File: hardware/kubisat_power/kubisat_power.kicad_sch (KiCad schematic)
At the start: 79 parts, among them J1 USB_C_Receptacle_PowerOnly_6P, Q1 Si2305, SW1 SW_Wuerth_450301014042, U1 TPS79601DCQ, U2 INA3221, U3 LN2220, U4 CN3791, U5 TP4056, U6 DW01A, U7 FS8205

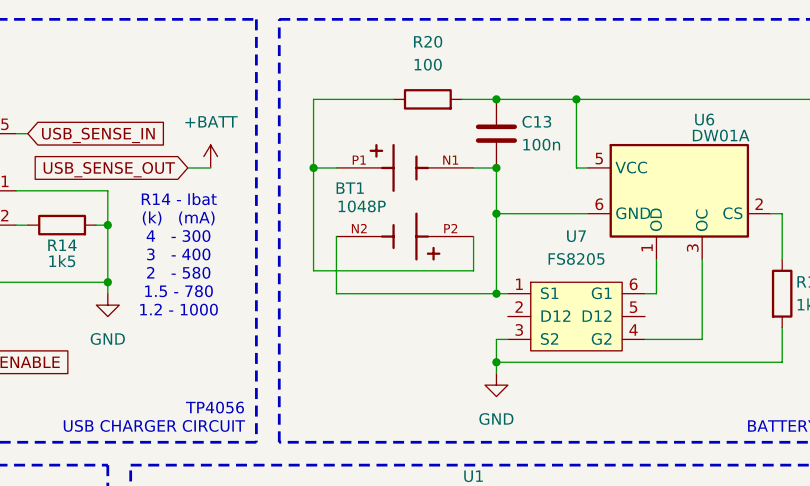
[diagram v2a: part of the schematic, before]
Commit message: changed battery holder
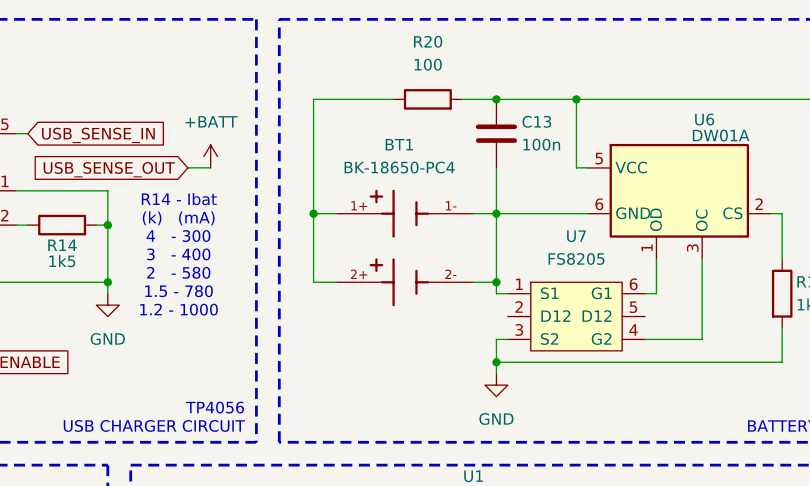
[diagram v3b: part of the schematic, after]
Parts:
- removed BT1: 1048P, 1048P:BAT_1048P, symbol 1048P:1048P
- added BT1: BK-18650-PC4, BK-18650-PC4:BAT_BK-18650-PC4, symbol kubisat:BK-18650-PC4
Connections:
- net at C13.2, U6.6 (GND), U7.1 (S1): now also BT1.1-, BT1.2-
- net at R20.1: now also BT1.1+, BT1.2+
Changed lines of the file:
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@@
 	)
 	(junction
+		(at 167.64 44.45)
+		(diameter 0)
+		(color 0 0 0 0)
+	)
+	(junction
 		(at 252.73 77.47)
 		(diameter 0)
@@
 	)
 	(junction
-		(at 147.32 31.75)
-		(diameter 0)
-		(color 0 0 0 0)
-	)
-	(junction
 		(at 165.1 88.9)
 		(diameter 0)
@@
 	)
 	(junction
-		(at 167.64 31.75)
-		(diameter 0)
-		(color 0 0 0 0)
-	)
-	(junction
 		(at 243.84 107.95)
 		(diameter 0)
@@
 	)
 	(junction
+		(at 147.32 36.83)
+		(diameter 0)
+		(color 0 0 0 0)
+	)
+	(junction
 		(at 259.08 27.94)
 		(diameter 0)
@@
 	)
 	(junction
-		(at 167.64 45.72)
-		(diameter 0)
-		(color 0 0 0 0)
-	)
-	(junction
 		(at 238.76 115.57)
 		(diameter 0)
@@
 	(wire
 		(pts
+			(xy 167.64 44.45) (xy 167.64 45.72)
+		)
+		(stroke
+			(width 0)
+			(type default)
+		)
+	)
+	(wire
+		(pts
 			(xy 214.63 137.16) (xy 212.09 137.16)
 		)
@@
 	(wire
 		(pts
-			(xy 167.64 45.72) (xy 149.86 45.72)
-		)
-		(stroke
-			(width 0)
-			(type default)
-		)
-	)
-	(wire
-		(pts
 			(xy 222.25 39.37) (xy 222.25 41.91)
 		)
@@
 	(wire
 		(pts
-			(xy 149.86 45.72) (xy 149.86 39.37)
-		)
-		(stroke
-			(width 0)
-			(type default)
-		)
-	)
-	(wire
-		(pts
 			(xy 53.34 111.76) (xy 53.34 115.57)
 		)
@@
 	(wire
 		(pts
+			(xy 147.32 44.45) (xy 149.86 44.45)
+		)
+		(stroke
+			(width 0)
+			(type default)
+		)
+	)
+	(wire
+		(pts
 			(xy 168.91 154.94) (xy 168.91 153.67)
 		)
@@
 	(wire
 		(pts
+			(xy 165.1 44.45) (xy 167.64 44.45)
+		)
+		(stroke
+			(width 0)
+			(type default)
+		)
+	)
+	(wire
+		(pts
 			(xy 67.31 54.61) (xy 67.31 52.07)
 		)
@@
 	(wire
 		(pts
-			(xy 147.32 31.75) (xy 147.32 24.13)
+			(xy 147.32 24.13) (xy 147.32 36.83)
 		)
 		(stroke
@@
 	(wire
 		(pts
-			(xy 147.32 43.18) (xy 165.1 43.18)
-		)
-		(stroke
-			(width 0)
-			(type default)
-		)
-	)
-	(wire
-		(pts
 			(xy 168.91 144.78) (xy 168.91 146.05)
 		)
@@
 	(wire
 		(pts
-			(xy 165.1 31.75) (xy 167.64 31.75)
-		)
-		(stroke
-			(width 0)
-			(type default)
-		)
-	)
-	(wire
-		(pts
 			(xy 233.68 154.94) (xy 238.76 154.94)
 		)
@@
 	(wire
 		(pts
+			(xy 147.32 36.83) (xy 147.32 44.45)
+		)
+		(stroke
+			(width 0)
+			(type default)
+		)
+	)
+	(wire
+		(pts
 			(xy 87.63 72.39) (xy 88.9 72.39)
 		)
@@
 	(wire
 		(pts
-			(xy 165.1 39.37) (xy 165.1 43.18)
-		)
-		(stroke
-			(width 0)
-			(type default)
-		)
-	)
-	(wire
-		(pts
-			(xy 167.64 36.83) (xy 167.64 45.72)
-		)
-		(stroke
-			(width 0)
-			(type default)
-		)
-	)
-	(wire
-		(pts
 			(xy 176.53 146.05) (xy 168.91 146.05)
 		)
@@
 	(wire
 		(pts
-			(xy 147.32 31.75) (xy 147.32 43.18)
-		)
-		(stroke
-			(width 0)
-			(type default)
-		)
-	)
-	(wire
-		(pts
 			(xy 205.74 22.86) (xy 205.74 24.13)
 		)
@@
 	(wire
 		(pts
-			(xy 167.64 31.75) (xy 167.64 36.83)
-		)
-		(stroke
-			(width 0)
-			(type default)
-		)
-	)
-	(wire
-		(pts
 			(xy 119.38 73.66) (xy 119.38 76.2)
 		)
@@
 	(wire
 		(pts
-			(xy 149.86 31.75) (xy 147.32 31.75)
+			(xy 149.86 36.83) (xy 147.32 36.83)
 		)
 		(stroke
@@
 	(wire
 		(pts
+			(xy 165.1 36.83) (xy 167.64 36.83)
+		)
+		(stroke
+			(width 0)
+			(type default)
+		)
+	)
+	(wire
+		(pts
 			(xy 180.34 128.27) (xy 179.07 128.27)
 		)
@@
 	(wire
 		(pts
+			(xy 167.64 36.83) (xy 167.64 31.75)
+		)
+		(stroke
+			(width 0)
+			(type default)
+		)
+	)
+	(wire
+		(pts
 			(xy 238.76 154.94) (xy 238.76 151.13)
 		)
@@
 	(wire
 		(pts
+			(xy 167.64 36.83) (xy 167.64 44.45)
+		)
+		(stroke
+			(width 0)
+			(type default)
+		)
+	)
+	(wire
+		(pts
 			(xy 278.13 26.67) (xy 278.13 30.48)
 		)
@@
 	)
 	(symbol
-		(lib_id "1048P:1048P")
-		(at 157.48 34.29 0)
+		(lib_id "kubisat:BK-18650-PC4")
+		(at 157.48 39.37 0)
 		(unit 1)
 		(exclude_from_sim no)
@@
 		(on_board yes)
 		(dnp no)
+		(fields_autoplaced yes)
 		(property "Reference" "BT1"
-			(at 151.384 34.036 0)
+			(at 156.845 29.21 0)
 			(effects
 				(font
@@
 			)
 		)
-		(property "Value" "1048P"
-			(at 152.654 36.068 0)
+		(property "Value" "BK-18650-PC4"
+			(at 156.845 31.75 0)
 			(effects
 				(font
@@
 			)
 		)
-		(property "Footprint" "1048P:BAT_1048P"
-			(at 157.48 34.29 0)
+		(property "Footprint" "BK-18650-PC4:BAT_BK-18650-PC4"
+			(at 157.48 39.37 0)
 			(effects
 				(font
@@
 		)
 		(property "Datasheet" ""
-			(at 157.48 34.29 0)
+			(at 157.48 39.37 0)
 			(effects
 				(font
@@
 		)
 		(property "Description" ""
-			(at 157.48 34.29 0)
+			(at 157.48 39.37 0)
 			(effects
 				(font
@@
 			)
 		)
-		(property "MF" "Keystone Electronics"
-			(at 157.48 34.29 0)
+		(property "MF" "MPD (Memory Protection Devices)"
+			(at 157.48 39.37 0)
 			(effects
 				(font
@@
 			)
 		)
-		(property "MAXIMUM_PACKAGE_HEIGHT" "14.85mm"
-			(at 157.48 34.29 0)
+		(property "MAXIMUM_PACKAGE_HEIGHT" "21.54 mm"
+			(at 157.48 39.37 0)
 			(effects
 				(font
@@
 		)
 		(property "Package" "None"
-			(at 157.48 34.29 0)
+			(at 157.48 39.37 0)
 			(effects
 				(font
@@
 		)
 		(property "Price" "None"
-			(at 157.48 34.29 0)
+			(at 157.48 39.37 0)
 			(effects
 				(font
@@
 			)
 		)
-		(property "Check_prices" "https://www.snapeda.com/parts/1048P/Keystone+Electronics/view-part/?ref=eda"
-			(at 157.48 34.29 0)
+		(property "Check_prices" "https://www.snapeda.com/parts/BK-18650-PC4/Memory+Protection+Devices/view-part/?ref=eda"
+			(at 157.48 39.37 0)
 			(effects
 				(font
@@
 		)
 		(property "STANDARD" "Manufacturer Recommendations"
-			(at 157.48 34.29 0)
-			(effects
-				(font
-					(size 1.27 1.27)
-				)
-				(justify bottom)
-				(hide yes)
-			)
-		)
-		(property "PARTREV" "A"
-			(at 157.48 34.29 0)
-			(effects
-				(font
-					(size 1.27 1.27)
-				)
-				(justify bottom)
-				(hide yes)
-			)
-		)
-		(property "SnapEDA_Link" "https://www.snapeda.com/parts/1048P/Keystone+Electronics/view-part/?ref=snap"
-			(at 157.48 34.29 0)
+			(at 157.48 39.37 0)
 			(effects
 				(font
@@
 			)
 		)
-		(property "MP" "1048P"
-			(at 157.48 34.29 0)
+		(property "PARTREV" "K"
+			(at 157.48 39.37 0)
 			(effects
 				(font
@@
 			)
 		)
-		(property "Purchase-URL" "https://www.snapeda.com/api/url_track_click_mouser/?unipart_id=625723&manufacturer=Keystone Electronics&part_name=1048P&search_term=None"
-			(at 157.48 34.29 0)
+		(property "SnapEDA_Link" "https://www.snapeda.com/parts/BK-18650-PC4/Memory+Protection+Devices/view-part/?ref=snap"
+			(at 157.48 39.37 0)
 			(effects
 				(font
@@
 			)
 		)
-		(property "Description_1" "\nSMT Polarized Battery Holder for Dual 18650 Batteries | Keystone Electronics 1048P\n"
-			(at 157.48 34.29 0)
+		(property "MP" "BK-18650-PC4"
+			(at 157.48 39.37 0)
 			(effects
 				(font
@@
 			)
 		)
-		(property "MANUFACTURER" "Keystone"
-			(at 157.48 34.29 0)
+		(property "Description_1" "\nBattery Holder (Open) 18650 2 Cell PC Pin\n"
+			(at 157.48 39.37 0)
 			(effects
 				(font
@@
 		)
 		(property "Availability" "In Stock"
-			(at 157.48 34.29 0)
+			(at 157.48 39.37 0)
 			(effects
 				(font
@@
 			)
 		)
-		(property "SNAPEDA_PN" "1048P"
-			(at 157.48 34.29 0)
+		(property "MANUFACTURER" "MPD"
+			(at 157.48 39.37 0)
 			(effects
 				(font
@@
 			)
 		)
-		(pin "N2"
+		(pin "2+"
 		)
-		(pin "N1"
+		(pin "2-"
 		)
-		(pin "P1"
+		(pin "1-"
 		)
-		(pin "P2"
+		(pin "1+"
 		)
 		(instances

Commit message: changed battery holder
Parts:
- BT1: footprint BK-18650-PC4:BAT_BK-18650-PC4 -> Library:BAT_BK-18650-PC4
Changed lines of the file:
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@@
 			)
 		)
-		(property "Footprint" "BK-18650-PC4:BAT_BK-18650-PC4"
+		(property "Footprint" "Library:BAT_BK-18650-PC4"
 			(at 157.48 39.37 0)
 			(effects

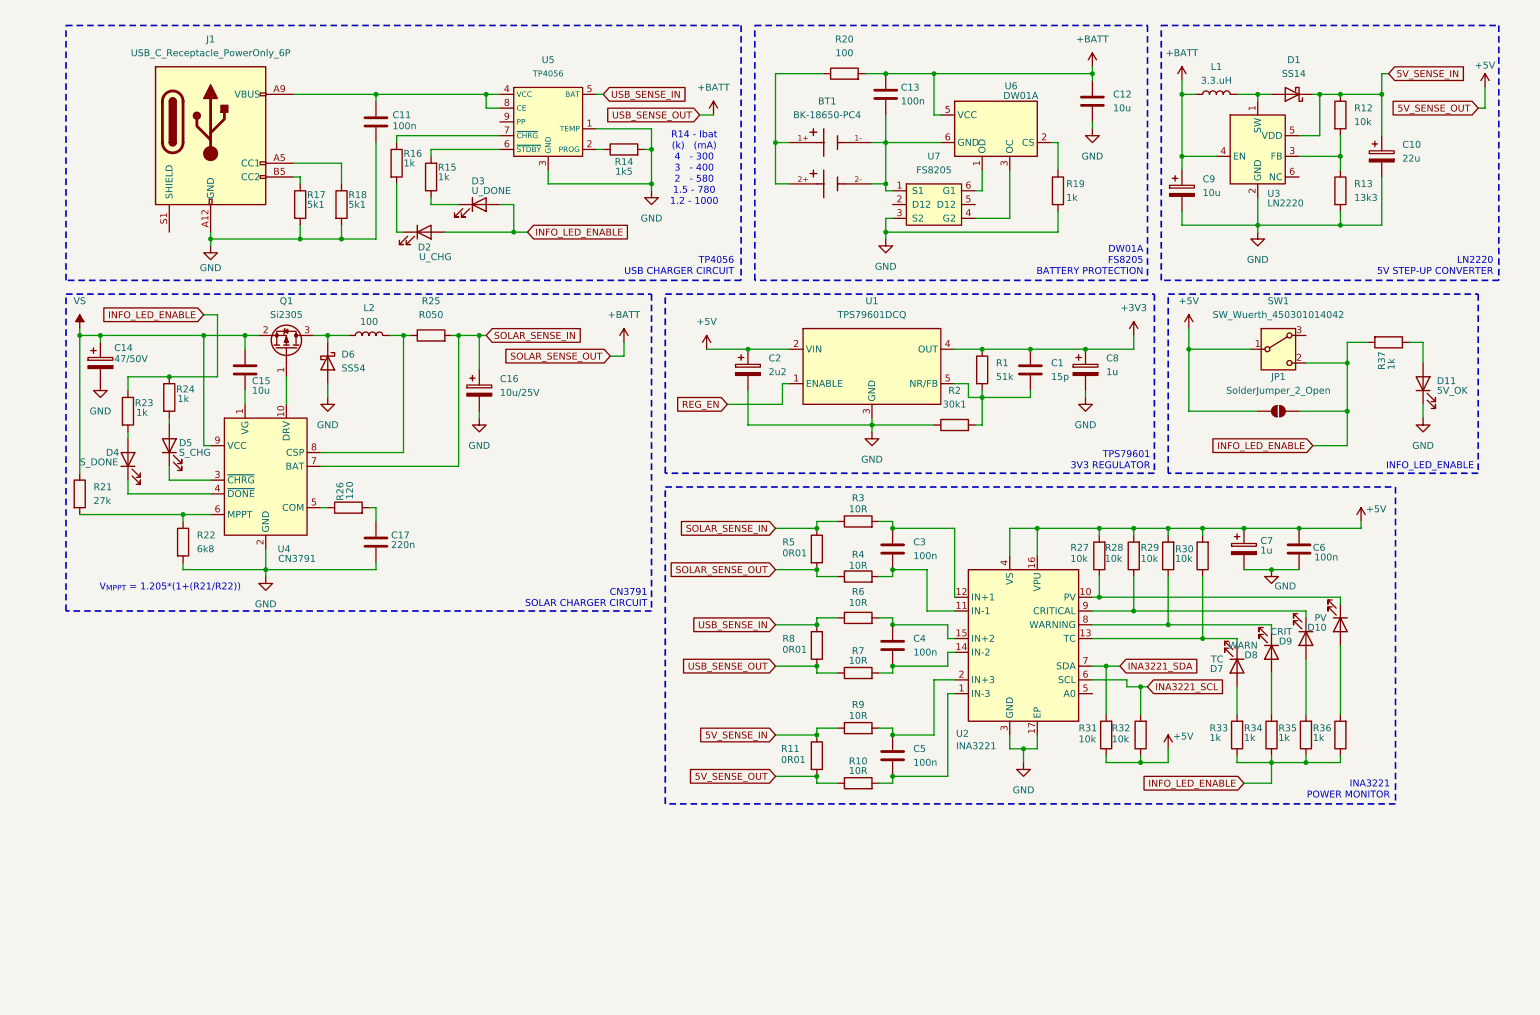
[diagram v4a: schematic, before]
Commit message: completed schematic with solar connectors, changed 3v3 regulator
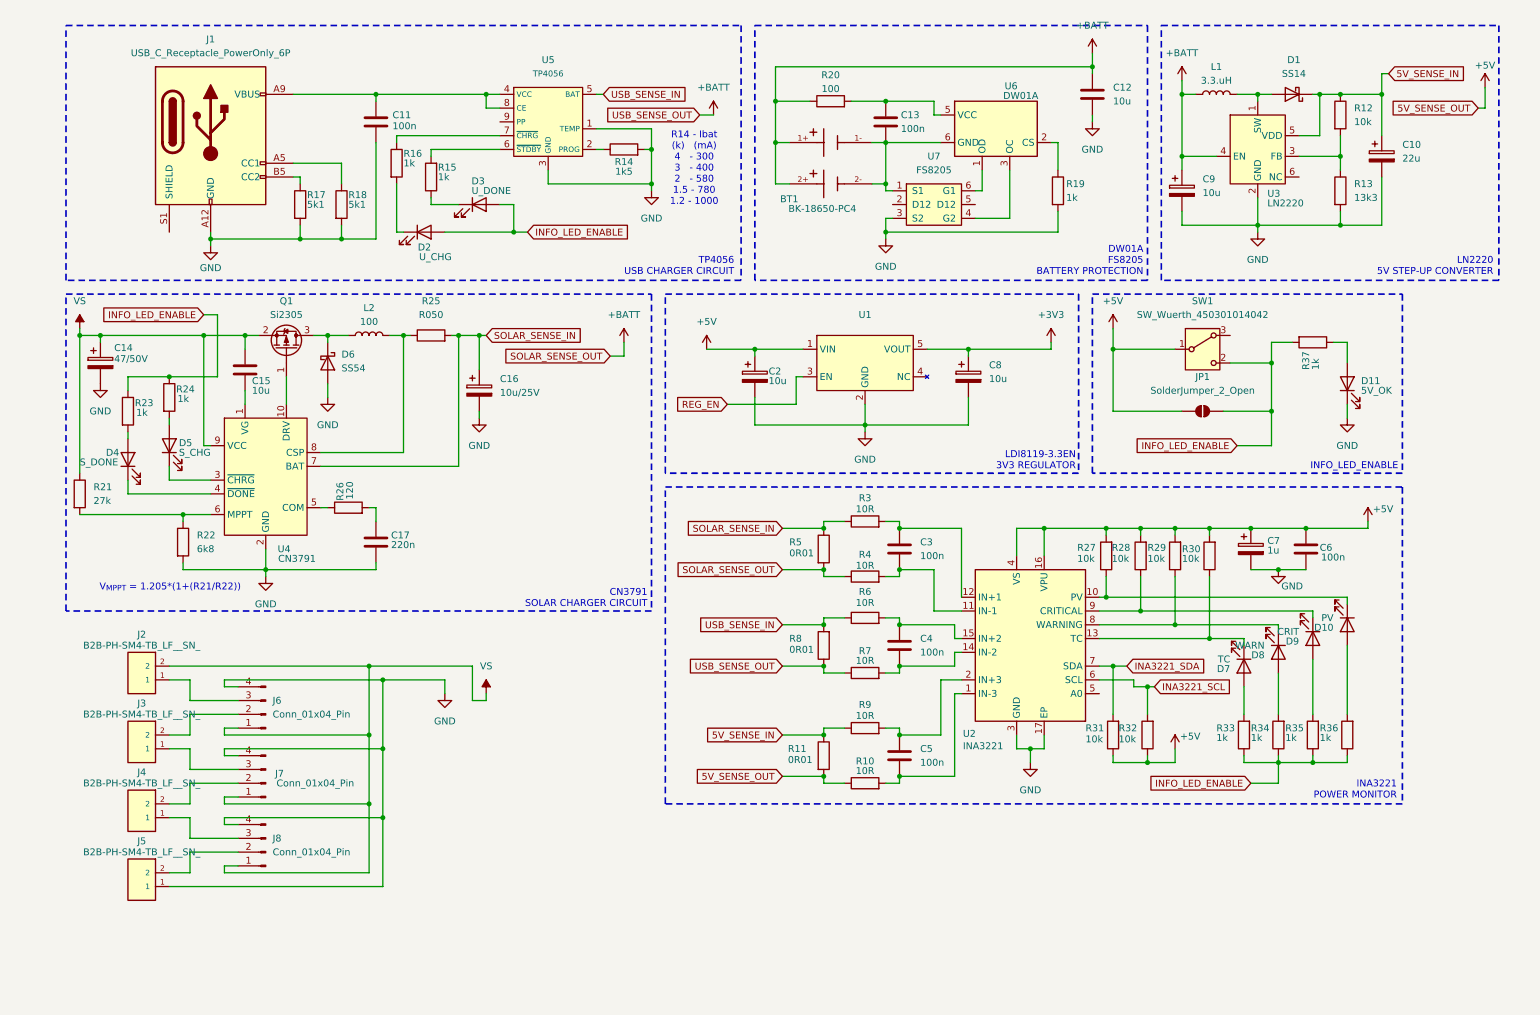
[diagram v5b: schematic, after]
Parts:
- removed C1: 15p, Capacitor_SMD:C_0805_2012Metric, symbol Device:C
- removed R1: 51k, Resistor_SMD:R_0805_2012Metric, symbol Device:R
- removed R2: 30k1, Resistor_SMD:R_0805_2012Metric, symbol Device:R
- removed U1: TPS79601DCQ, Package_TO_SOT_SMD:SOT-223-6_TabPin3, symbol kubisat:TPS79601
- added J2, J3, J4, J5: B2B-PH-SM4-TB_LF__SN_, kubisat:B2B-PH-SM4-TB_LF__SN_, symbol kubisat:B2B-PH-SM4-TB_LF__SN_
- added J6, J7, J8: Conn_01x04_Pin, Connector_PinHeader_2.54mm:PinHeader_1x04_P2.54mm_Vertical, symbol Connector:Conn_01x04_Pin
- added U1: ~, Package_TO_SOT_SMD:SOT-23-5, symbol kubisat:LDI8119-3.3EN
- C2: value 2u2 -> 10u
- C8: value 1u -> 10u
- R19, R20: footprint Resistor_SMD:R_2512_6332Metric_Pad1.40x3.35mm_HandSolder -> Resistor_SMD:R_0805_2012Metric
- U7: footprint Package_TO_SOT_SMD:SOT-23-6 -> Package_SO:TSSOP-8_3x3mm_P0.65mm
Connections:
- net +3V3: now also U1.5 (VOUT)
- net +5V: now also U1.1 (VIN)
- net +BATT: now also BT1.1+, BT1.2+, R20.1; no longer C13.1, R20.2, U6.5 (VCC)
- net GND: now also J5.1, J6.4 (Pin_4), J7.4 (Pin_4), J8.4 (Pin_4), U1.2 (GND)
- net REG_EN: now also U1.3 (EN)
- net VS: now also J2.2, J6.1 (Pin_1), J7.1 (Pin_1), J8.1 (Pin_1)
- new net: J5.2, J8.2 (Pin_2)
- new net: J4.1, J8.3 (Pin_3)
- new net: J2.1, J6.3 (Pin_3)
- new net: J4.2, J7.2 (Pin_2)
- new net: C13.1, R20.2, U6.5 (VCC)
- new net: J3.2, J6.2 (Pin_2)
- new net: J3.1, J7.3 (Pin_3)
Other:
- note added: "LDI8119-3.3EN 3V3 REGULATOR"
- note removed: "TPS79601 3V3 REGULATOR"
- moved on the sheet: C12, C13, C2, C3, C4, C5, C6, C7, C8, D10, D11, D7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

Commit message: arranged elements on board, made some traces
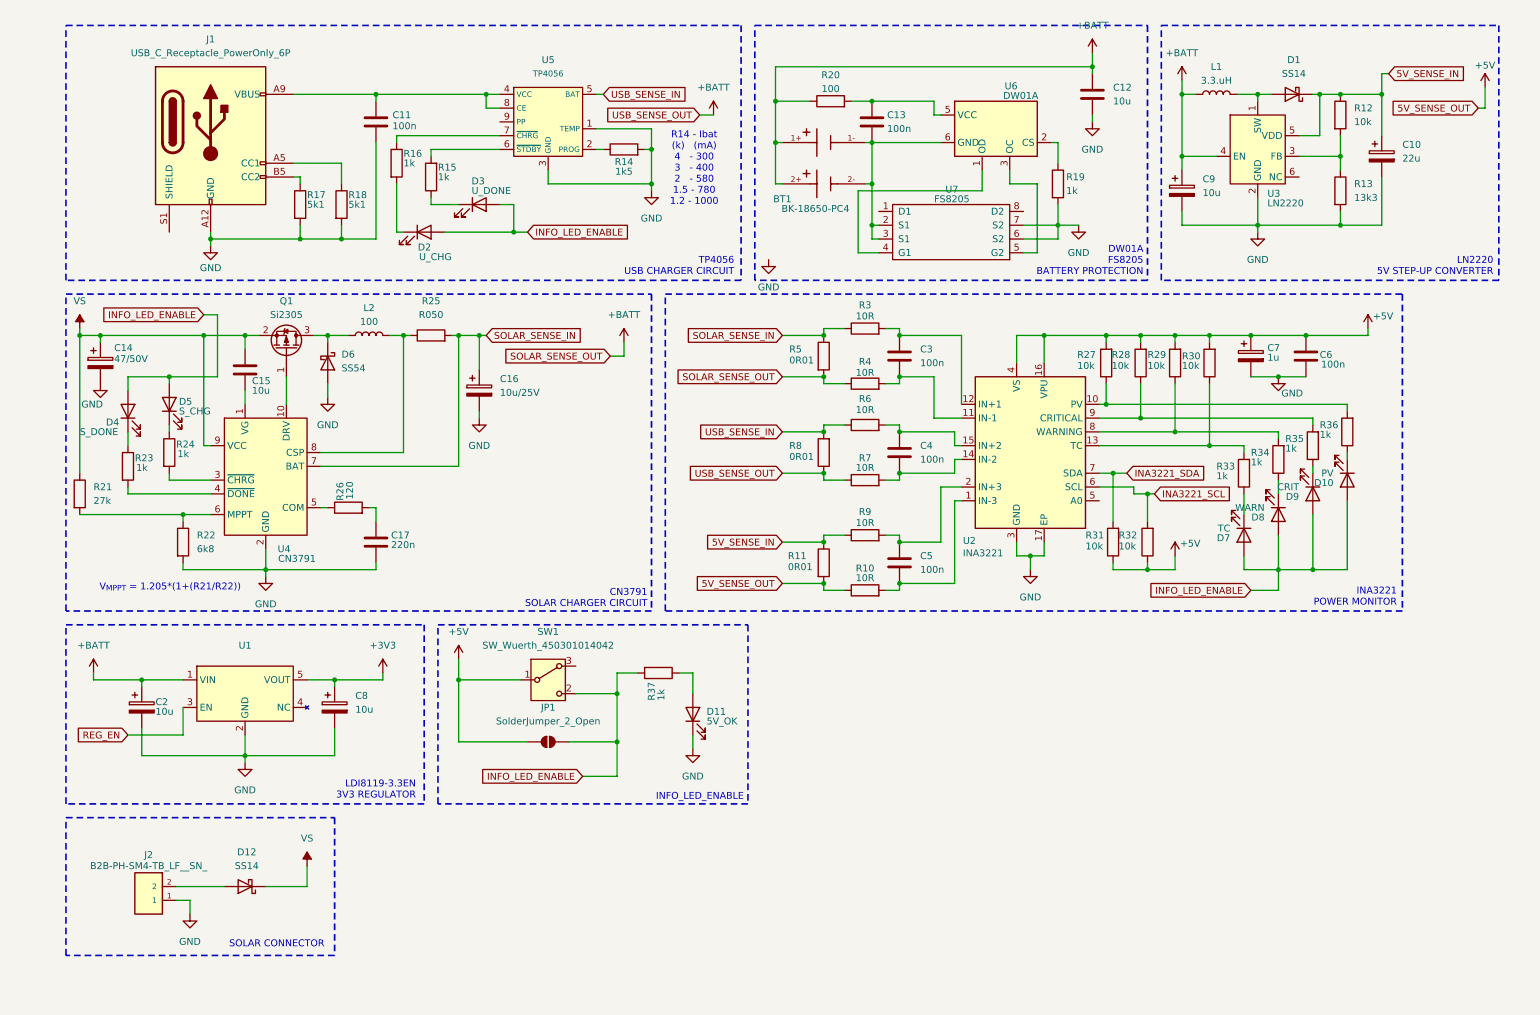
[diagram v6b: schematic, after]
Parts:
- removed J3, J4, J5: B2B-PH-SM4-TB_LF__SN_, kubisat:B2B-PH-SM4-TB_LF__SN_, symbol kubisat:B2B-PH-SM4-TB_LF__SN_
- removed J6, J7, J8: Conn_01x04_Pin, Connector_PinHeader_2.54mm:PinHeader_1x04_P2.54mm_Vertical, symbol Connector:Conn_01x04_Pin
- added D12: SS14, Diode_SMD:D_SMA, symbol Diode:SS14
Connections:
- net +5V: no longer C2.1, U1.1 (VIN)
- net +BATT: now also C2.1, U1.1 (VIN)
- net GND: now also J2.1, U7.6 (S2), U7.7 (S2); no longer U7.3 (S2)
- net INFO_LED_ENABLE: now also D10.2 (A), D4.2 (A), D5.2 (A), D7.2 (A), D8.2 (A), D9.2 (A); no longer R23.1, R24.1, R33.1, R34.1, R35.1, R36.1
- net VS: now also D12.1 (K); no longer J2.2
- net at R29.1, U2.8 (WARNING): now also R34.2; no longer D8.1 (K)
- net at R23.2: now also U4.4 (~{DONE}); no longer D4.2 (A)
- net at R24.2: now also U4.3 (~{CHRG}); no longer D5.2 (A)
- net at R30.1, U2.13 (TC): now also R33.2; no longer D7.1 (K)
- net at D4.1 (K): now also R23.1; no longer U4.4 (~{DONE})
- net at BT1.1-, BT1.2-, C13.2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: now also U7.2 (S1), U7.3 (S1); no longer U7.1 (S1)
- net at D5.1 (K): now also R24.1; no longer U4.3 (~{CHRG})
- net at R27.1, U2.10 (PV): now also R36.2; no longer D10.1 (K)
- net at U6.1 (OD): now also U7.4 (G1); no longer U7.6 (G1)
- net at U6.3 (OC): now also U7.5 (G2); no longer U7.4 (G2)
- net at R28.1, U2.9 (CRITICAL): now also R35.2; no longer D9.1 (K)
- new net: D8.1 (K), R34.1
- new net: D12.2 (A), J2.2
- new net: D10.1 (K), R36.1
- new net: D7.1 (K), R33.1
- new net: D9.1 (K), R35.1
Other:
- note added: "SOLAR CONNECTOR"
- moved on the sheet: BT1, C13, C2, C3, C4, C5, C6, C7, C8, D10, D11, D4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
